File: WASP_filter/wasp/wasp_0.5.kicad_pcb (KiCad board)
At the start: 2 copper layers, 50 x 80.5 mm, 61 parts, among them J1 INPUT_SWT, J2 RES_POT, J3 FLT_MODE_SWT, J4 CUT_POT, J5 OUT_SWT, J6 CV, J7 Eurorack_16_pin, U1 4069, U2 LM13700, U3 AMS1117-5.0

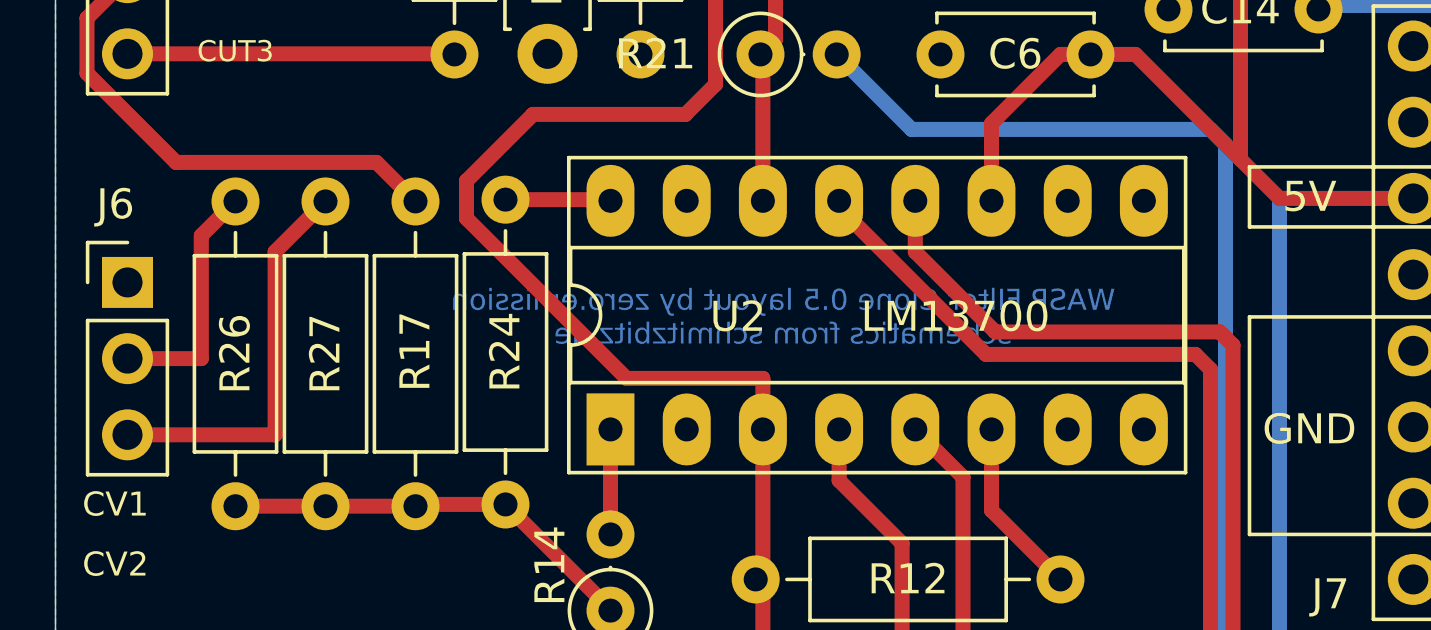
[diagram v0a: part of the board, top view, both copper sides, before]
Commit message: Corrections made to ground planes, trace widths, etc. after visual checks of printout
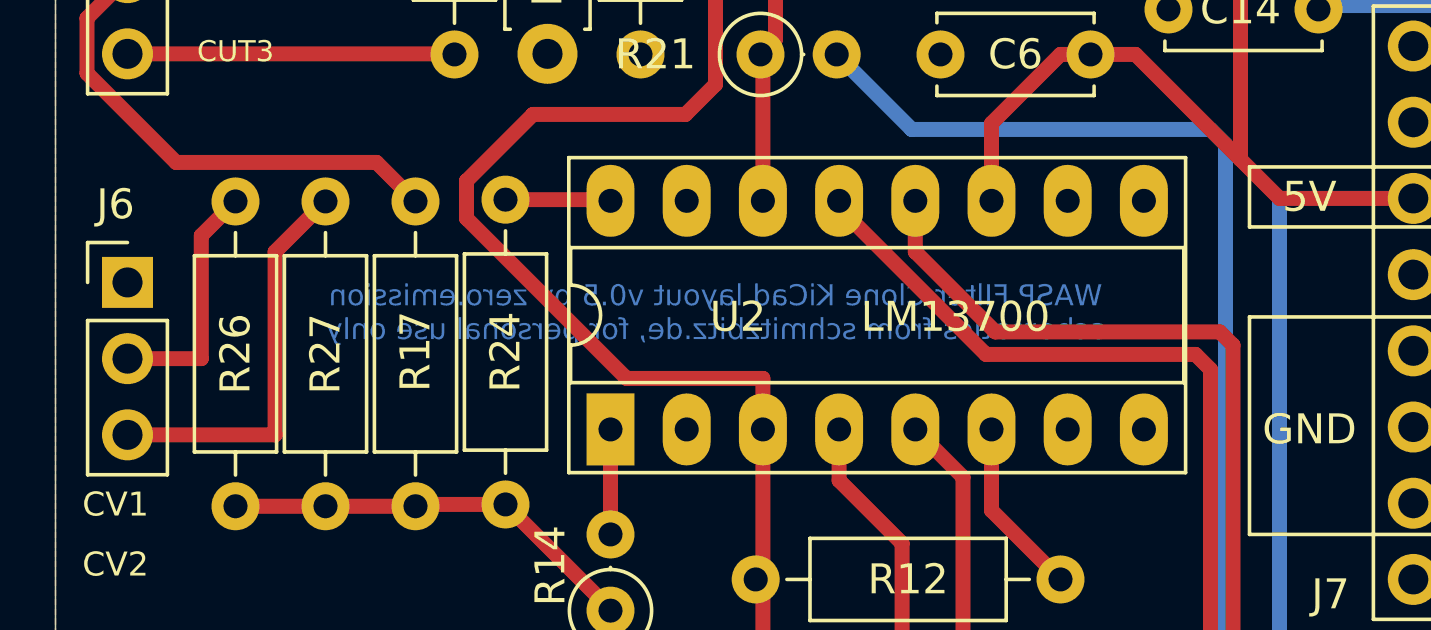
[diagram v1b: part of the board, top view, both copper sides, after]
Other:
- board text added: "WASP FIlter Clone KiCad layout v0.5 by zero.emission schematics from schmitzbitz.de, for personal use only"
- board text removed: "WASP FIlter Clone 0.5 layout by zero.emission schematics from schmitzbitz.de"
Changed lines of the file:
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@@
   (gr_line (start 99 127) (end 49 127) (layer Edge.Cuts) (width 0.05))
   (gr_line (start 49 127) (end 49 46.5) (layer Edge.Cuts) (width 0.05))
-  (gr_text "WASP FIlter Clone 0.5 layout by zero.emission\nschematics from schmitzbitz.de" (at 73.25 68.75) (layer B.Cu)
+  (gr_text "WASP FIlter Clone KiCad layout v0.5 by zero.emission\nschematics from schmitzbitz.de, for personal use only" (at 71 68.6) (layer B.Cu)
     (effects (font (size 0.7 0.7) (thickness 0.08)) (justify mirror))
   )
